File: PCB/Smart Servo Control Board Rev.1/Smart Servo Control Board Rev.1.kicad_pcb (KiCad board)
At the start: 4 copper layers, 36.8 x 16.5 mm, 37 parts, among them J1 PRGR, J2 CTRL, J3 CTRL, J4 MOT, J5 MOT, Q1 AO3400A, Q2 AO3400A, U1 AMS1117-3.3, U2 STM32F030C8Tx, U3 INA219AxD, U4 INA219AxD, U5 IRF7307, U6 AS5600, U7 IRF7307

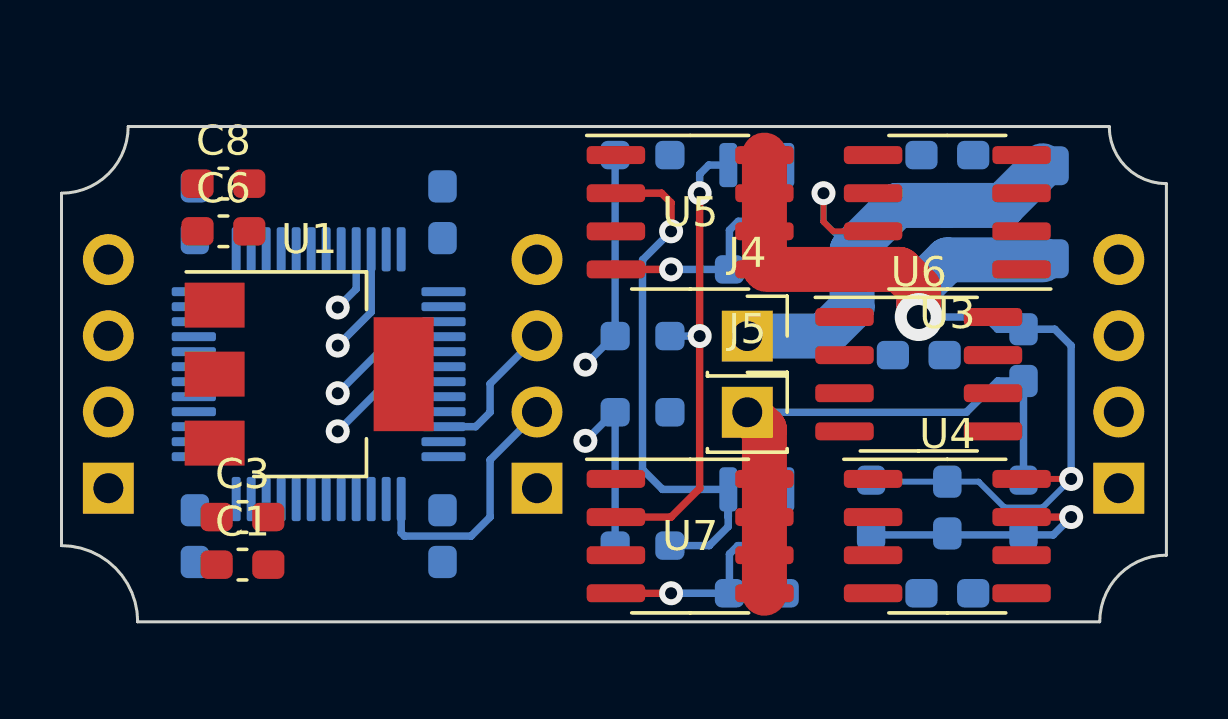
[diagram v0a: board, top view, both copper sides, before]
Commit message: Prima versione definitiva PCB
tracciate le piste nel modo migliore possibile per ora, resta da sistemare il silkscreen.
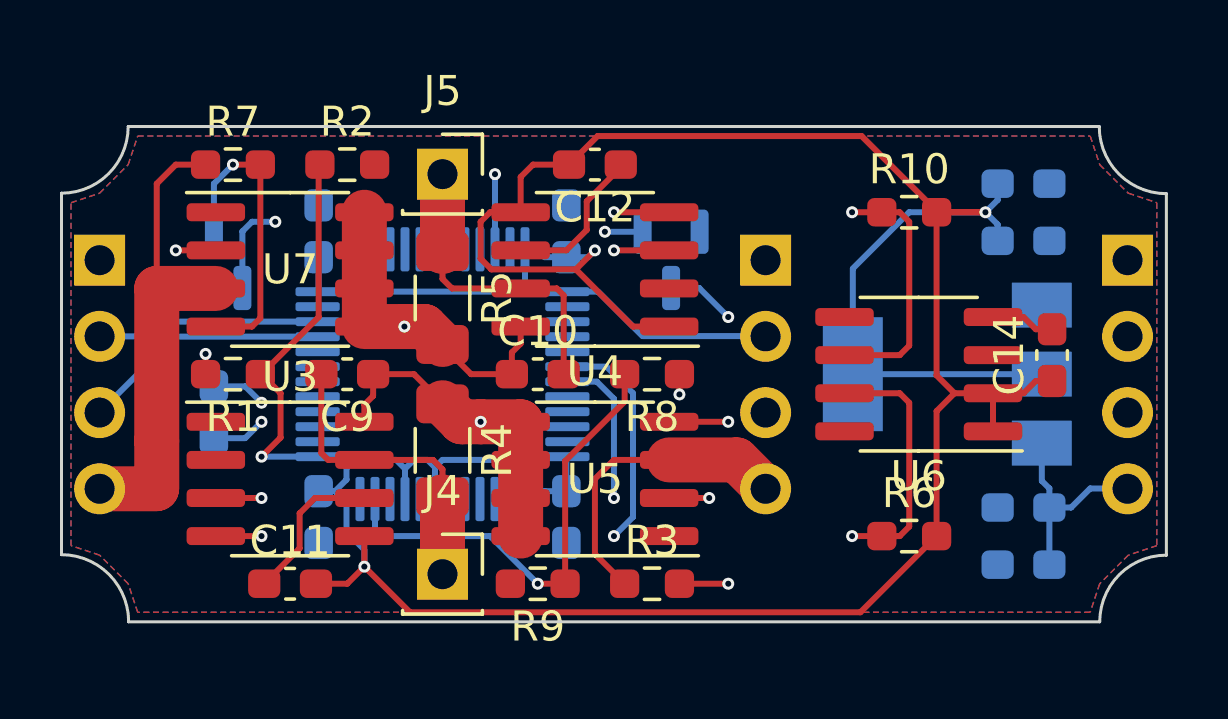
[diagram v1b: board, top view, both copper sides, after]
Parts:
- added R10: 10K, Resistor_SMD:R_0603_1608Metric_Pad0.98x0.95mm_HandSolder, F.Cu at (99.4, 30.8)
- C1, C3, C6, C8, U1: moved to B.Cu
- C10, C11, C12, C14, C9, R1, R2, R3, R6, R7, R8, R9: moved to F.Cu
- R4: value 0R1 -> 100m; moved to F.Cu
- R5: value 100R -> 100m; footprint Resistor_SMD:R_0603_1608Metric_Pad0.98x0.95mm_HandSolder -> Resistor_SMD:R_1206_3216Metric_Pad1.30x1.75mm_HandSolder; moved to F.Cu
- moved J2 34.8 mm to (72.4, 32.4), turned to 180 degrees
- moved J3 34.8 mm to (106.7, 32.4), turned to 180 degrees
- moved C13 27.1 mm to (76.2, 37.5), turned to 90 degrees
- moved C6 26.7 mm to (103.2, 31.8)
- moved C8 26.7 mm to (103.2, 29.8)
- moved C11 26.2 mm to (78.7, 43.2), turned to 0 degrees
- moved C1 26.1 mm to (103.2, 40.6), turned to 180 degrees
- moved C3 26.1 mm to (103.2, 42.5), turned to 180 degrees
- moved U3 23.6 mm to (78.7, 39.7), turned to 0 degrees
- moved R7 22.6 mm to (76.8, 29.2), turned to 0 degrees
- moved R4 21.5 mm to (83.8, 38.7), turned to -90 degrees
- moved U1 21.3 mm to (100.6, 36.2), turned to 180 degrees
- moved C9 20.6 mm to (80.6, 36.2), turned to 180 degrees
- moved Q2 20.0 mm to (76.2, 32.4), turned to 90 degrees
- moved C12 18.5 mm to (88.9, 29.2), turned to 180 degrees
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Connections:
- net I_SENS - renamed I_SENS_1 -
- C10 pad 1: I_SENS + -> I_SENS_2 +
- C10 pad 2: V_SENS - -> I_SENS_2 -
- C13 pad 1: I_SENS + -> I_SENS_1 +
- C13 pad 2: Net-(C13-Pad2) -> I_SENS_2 +
- C9 pad 1: I_SENS + -> I_SENS_1 +
- J5 pad 1: Net-(C13-Pad2) -> I_SENS_2 -
- R4 pad 1: I_SENS + -> I_SENS_1 +
- R5 pad 1: V_SENS - -> I_SENS_2 -
- R5 pad 2: I_SENS + -> I_SENS_2 +
- R6 pad 1: V_SENS - -> SCL1
- R6 pad 2: Net-(C13-Pad2) -> +3V3
- U2 pad 11: unconnected-(U2-Pad11) -> B
- U2 pad 13: unconnected-(U2-Pad13) -> A
- U2 pad 29: A -> unconnected-(U2-Pad29)
- U2 pad 31: B -> unconnected-(U2-Pad31)
- U3 pad 8: I_SENS + -> I_SENS_1 +
- U4 pad 1: GNDD -> +3V3
- U4 pad 2: +3V3 -> GNDD
- U4 pad 7: V_SENS - -> I_SENS_2 -
- U4 pad 8: I_SENS + -> I_SENS_2 +
- U5 pad 5: I_SENS + -> I_SENS_1 +
- U5 pad 6: I_SENS + -> I_SENS_1 +
- U5 pad 7: I_SENS + -> I_SENS_1 +
- U5 pad 8: I_SENS + -> I_SENS_1 +
- U7 pad 5: Net-(C13-Pad2) -> I_SENS_2 +
- U7 pad 6: Net-(C13-Pad2) -> I_SENS_2 +
- U7 pad 7: Net-(C13-Pad2) -> I_SENS_2 +
- U7 pad 8: Net-(C13-Pad2) -> I_SENS_2 +
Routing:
- net +3V3: track 0.00 -> 115.9 mm, vias 0 -> 3
- net SCL1: track 0.00 -> 50.4 mm, vias 0 -> 4
- net SDA1: track 0.00 -> 45.4 mm, vias 0 -> 4
- net I_SENS +: track 34.4 -> 0.00 mm, vias 2 -> 0
- net +5V: track 0.00 -> 33.6 mm
- net SCL2: track 10.2 -> 43.7 mm, vias 1 -> 0
- net SDA2: track 12.2 -> 42.8 mm, vias 1 -> 0
- net I_SENS_1 +: track 0.00 -> 20.2 mm, vias 0 -> 2
- net I_SENS_2 +: track 0.00 -> 19.6 mm, vias 0 -> 2
- net Net-(C13-Pad2): track 19.1 -> 0.00 mm
- net SWDIO: track 4.95 -> 21.5 mm, vias 0 -> 1
- net GNDD: track 0.00 -> 12.5 mm
- net I_SENS_2 -: track 0.00 -> 10.4 mm
- net B': track 18.8 -> 28.9 mm, vias 1 -> 3
- net Net-(Q1-Pad3): track 6.19 -> 14.8 mm, vias 1 -> 3
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- added copper zone on In1.Cu, net +5V
- added copper zone on B.Cu, net GNDD
- added copper zone on F.Cu, net GNDD
- added copper zone on In1.Cu, net GNDD
- added copper zone on In2.Cu, net GNDD
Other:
- outline, holes or cut-outs redrawn
